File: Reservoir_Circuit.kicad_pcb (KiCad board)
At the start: 2 copper layers, 70 x 57.5 mm, 17 parts, among them J1 CN7, J2 CN10, J3 ECE298_RS_PWR_EXT, U1 CD74HC540E, U2 HC-SR04

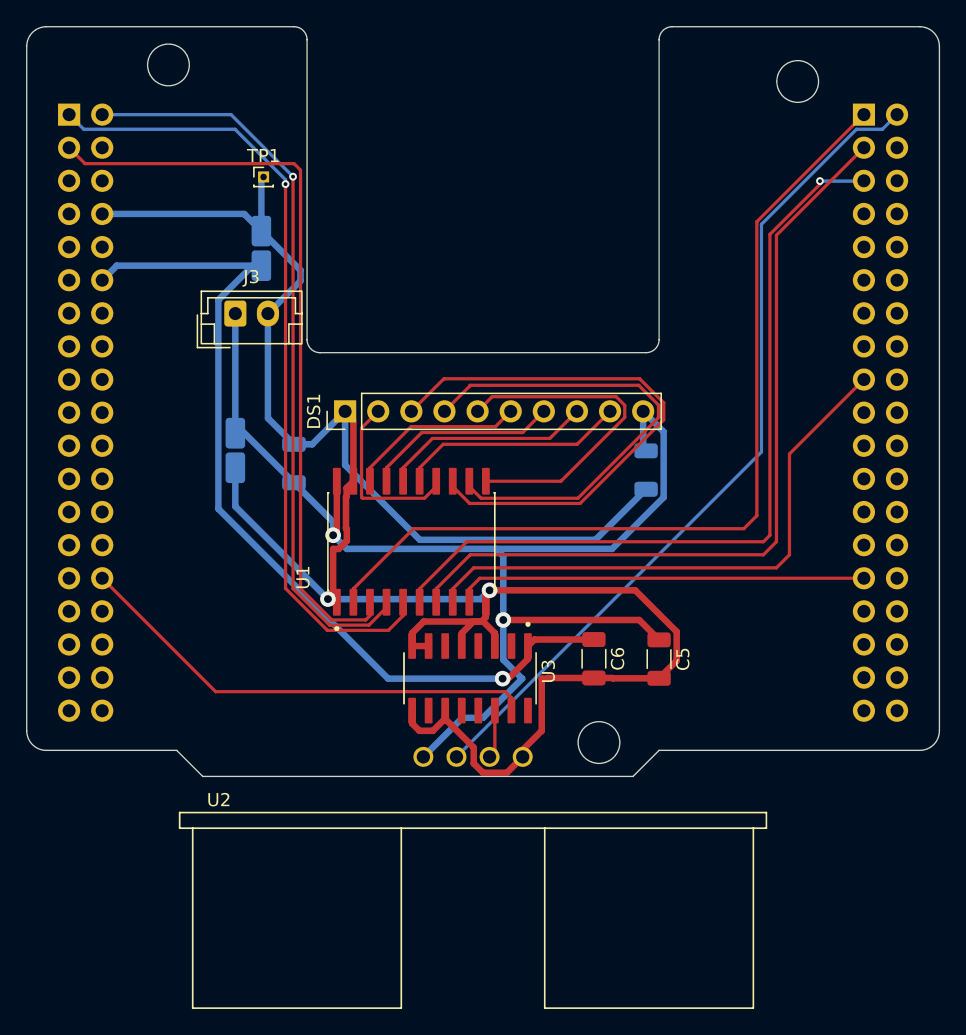
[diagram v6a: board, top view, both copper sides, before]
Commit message: Added servo and RGB LED hardware
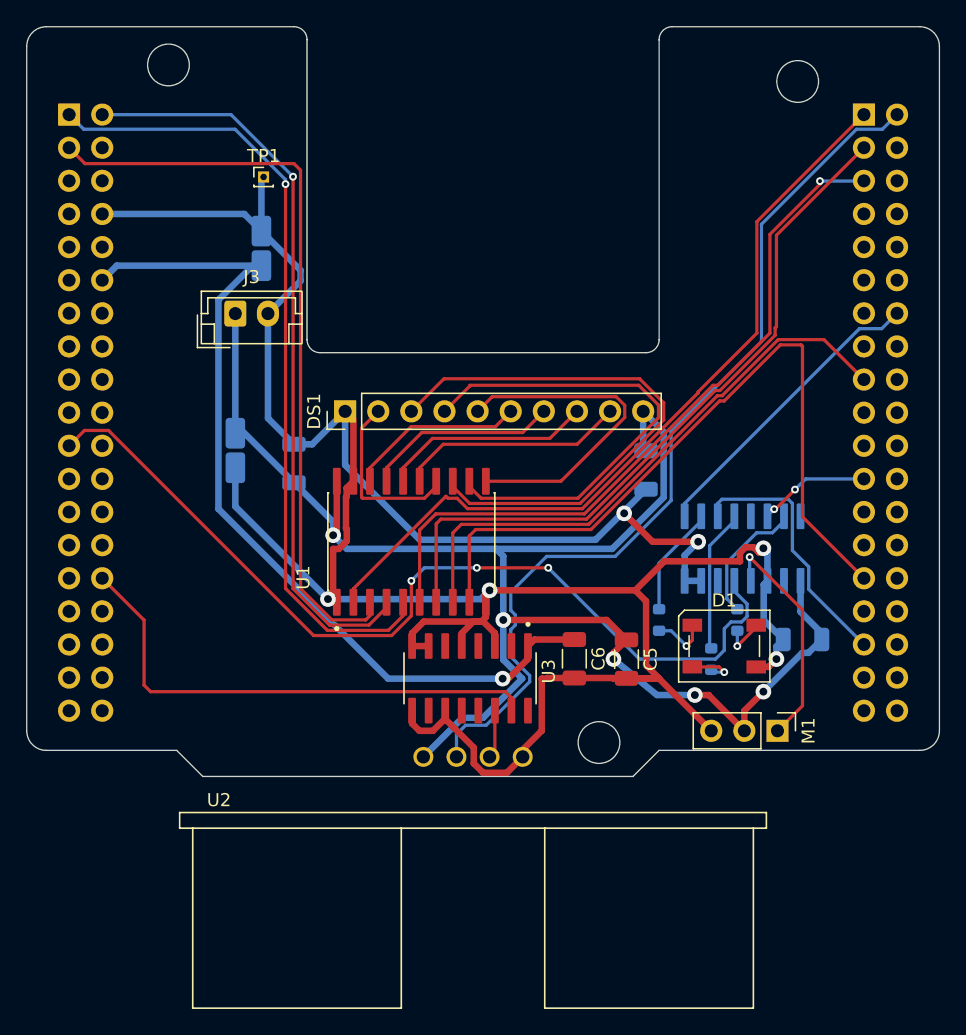
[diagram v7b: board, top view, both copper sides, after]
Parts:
- added C7: 10nF, Capacitor_SMD:C_1206_3216Metric, B.Cu at (161.0, 102.5)
- added D1: LED_GRKB, LED_SMD:LED_Inolux_IN-PI554FCH_PLCC4_5.0x5.0mm_P3.2mm, F.Cu at (155.0, 103.0)
- added M1: Motor_Servo, Connector_PinHeader_2.54mm:PinHeader_1x03_P2.54mm_Vertical, F.Cu at (159.1, 109.5)
- added R1: 100, PCM_SparkFun-Resistor:R_0603_1608Metric, B.Cu at (156.0, 101.0)
- added R2: 100, PCM_SparkFun-Resistor:R_0603_1608Metric, B.Cu at (154.0, 104.0)
- added R3: 100, PCM_SparkFun-Resistor:R_0603_1608Metric, B.Cu at (150.0, 101.0)
- added U4: ~, CD74HC4049MT:SOIC127P600X175-16N, B.Cu at (156.4, 95.5)
- moved C5 2.50 mm to (147.5, 104.0)
- moved C6 1.50 mm to (143.5, 104.0)
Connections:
- J1 pad 21: unconnected-(J1-Pin_21-Pad21) -> /PB7
- J2 pad 14: unconnected-(J2-Pin_14-Pad14) -> /PA11
- J2 pad 23: unconnected-(J2-Pin_23-Pad23) -> /PA8
- J2 pad 33: unconnected-(J2-Pin_33-Pad33) -> /PA10
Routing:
- net /PB7: track 0.00 -> 71.1 mm, vias 0 -> 3
- net GND: track 178.7 -> 220.3 mm, vias 2 -> 6
- net +5V_EXT: track 96.4 -> 122.9 mm, vias 2 -> 5
- net /PB5: track 31.6 -> 56.5 mm
- net /PA11: track 0.00 -> 23.3 mm
- net /PA10: track 0.00 -> 20.1 mm
- net /SERVO_SIG: track 0.00 -> 17.7 mm, vias 0 -> 1
- net /R_BUF: track 0.00 -> 11.0 mm
- net /B_BUF: track 0.00 -> 9.98 mm
- net /PA8: track 0.00 -> 8.61 mm, vias 0 -> 2
- net /G_BUF: track 0.00 -> 8.46 mm
- net /PC9: track 68.5 -> 61.1 mm
- net /PB9: track 61.7 -> 55.3 mm
- net /PB8: track 61.6 -> 55.2 mm
- net /PC8: track 64.4 -> 69.9 mm
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
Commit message: Added motor and motor driver
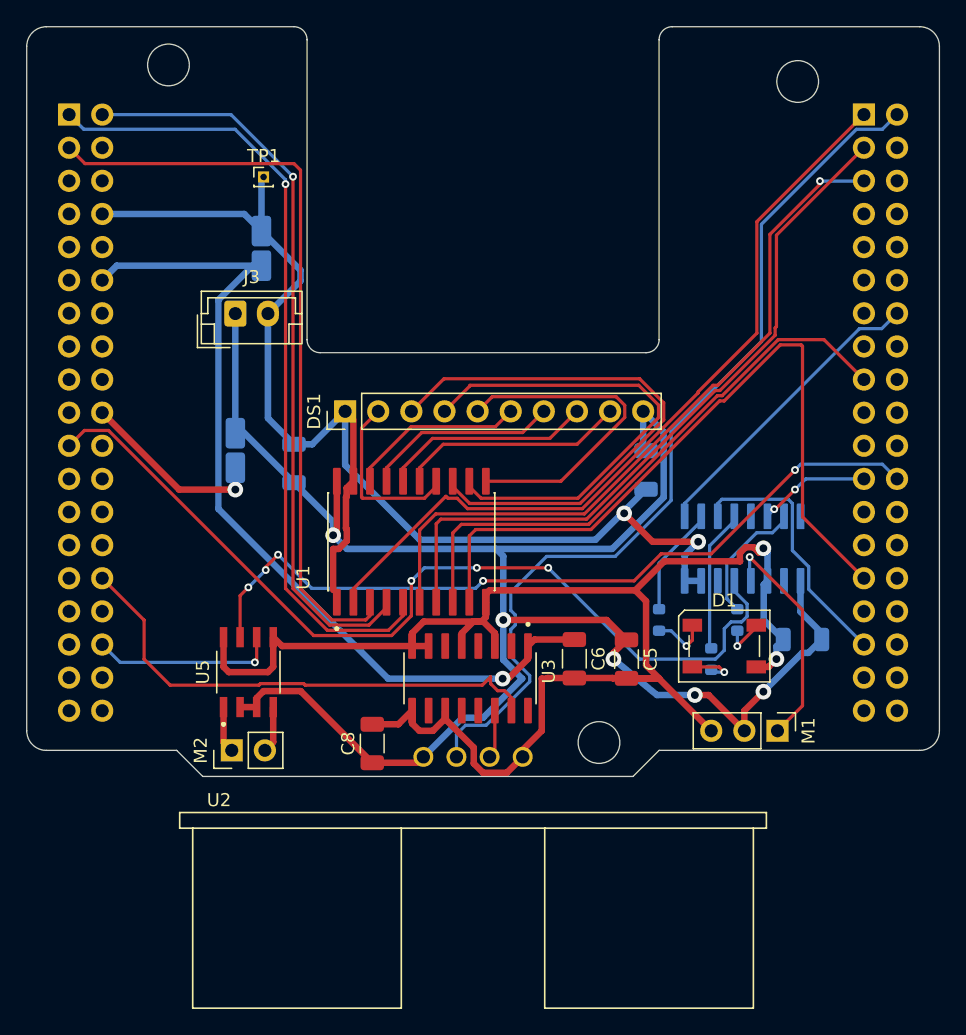
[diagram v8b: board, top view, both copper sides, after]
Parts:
- added C8: 10nF, Capacitor_SMD:C_1206_3216Metric, F.Cu at (128.0, 110.5)
- added M2: Motor_DC, Connector_PinHeader_2.54mm:PinHeader_1x02_P2.54mm_Vertical, F.Cu at (117.2, 111.0)
- added U5: L9110S, L9110S:SOIC127P599X172-8N, F.Cu at (118.5, 105.0)
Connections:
- J1 pad 34: unconnected-(J1-Pin_34-Pad34) -> /PB0
- J2 pad 24: unconnected-(J2-Pin_24-Pad24) -> /PB1
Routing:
- net /PB1: track 0.00 -> 60.5 mm, vias 0 -> 5
- net +5V_EXT: track 122.9 -> 140.3 mm
- net /PB0: track 0.00 -> 14.3 mm, vias 0 -> 1
- net GND: track 220.3 -> 231.3 mm, vias 6 -> 5
- net /OB: track 0.00 -> 3.59 mm
- net /OA: track 0.00 -> 3.58 mm
